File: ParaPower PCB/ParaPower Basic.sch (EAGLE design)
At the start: 4 parts, among them U1 ESP32_ESP-WROOM-32

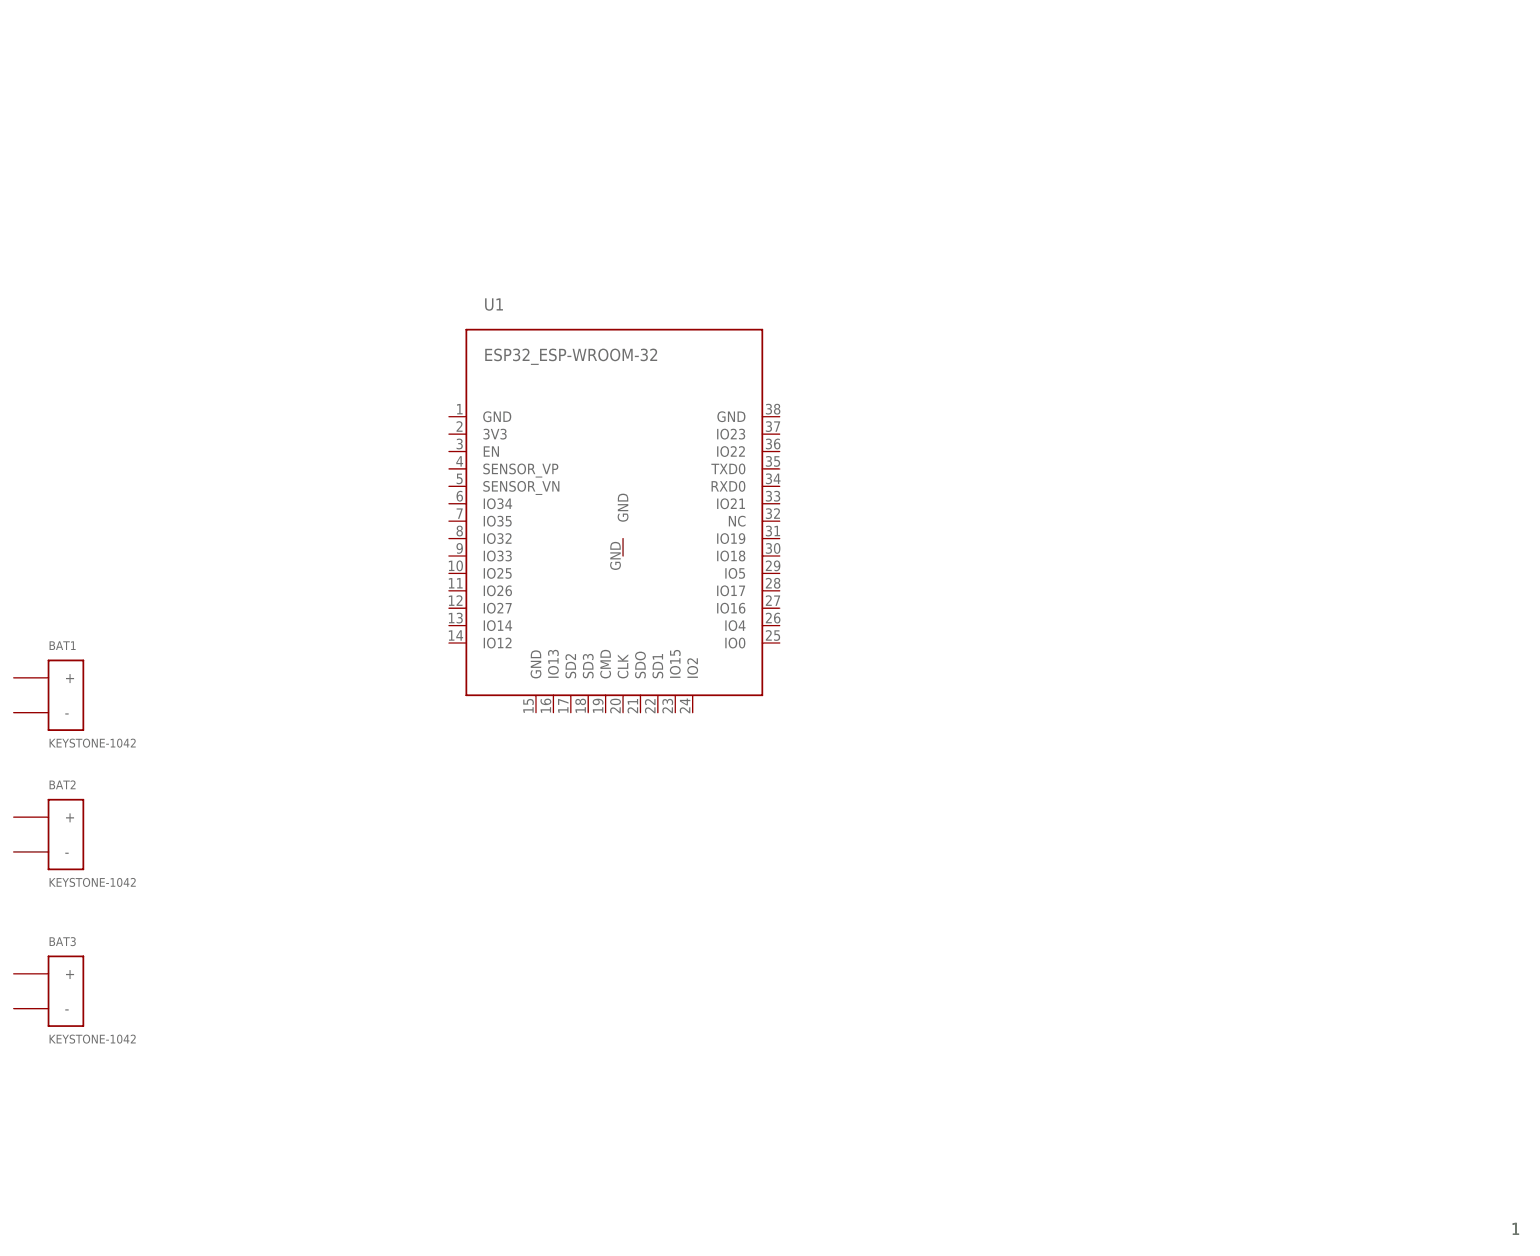
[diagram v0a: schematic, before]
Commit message: started to add voltage regulation section
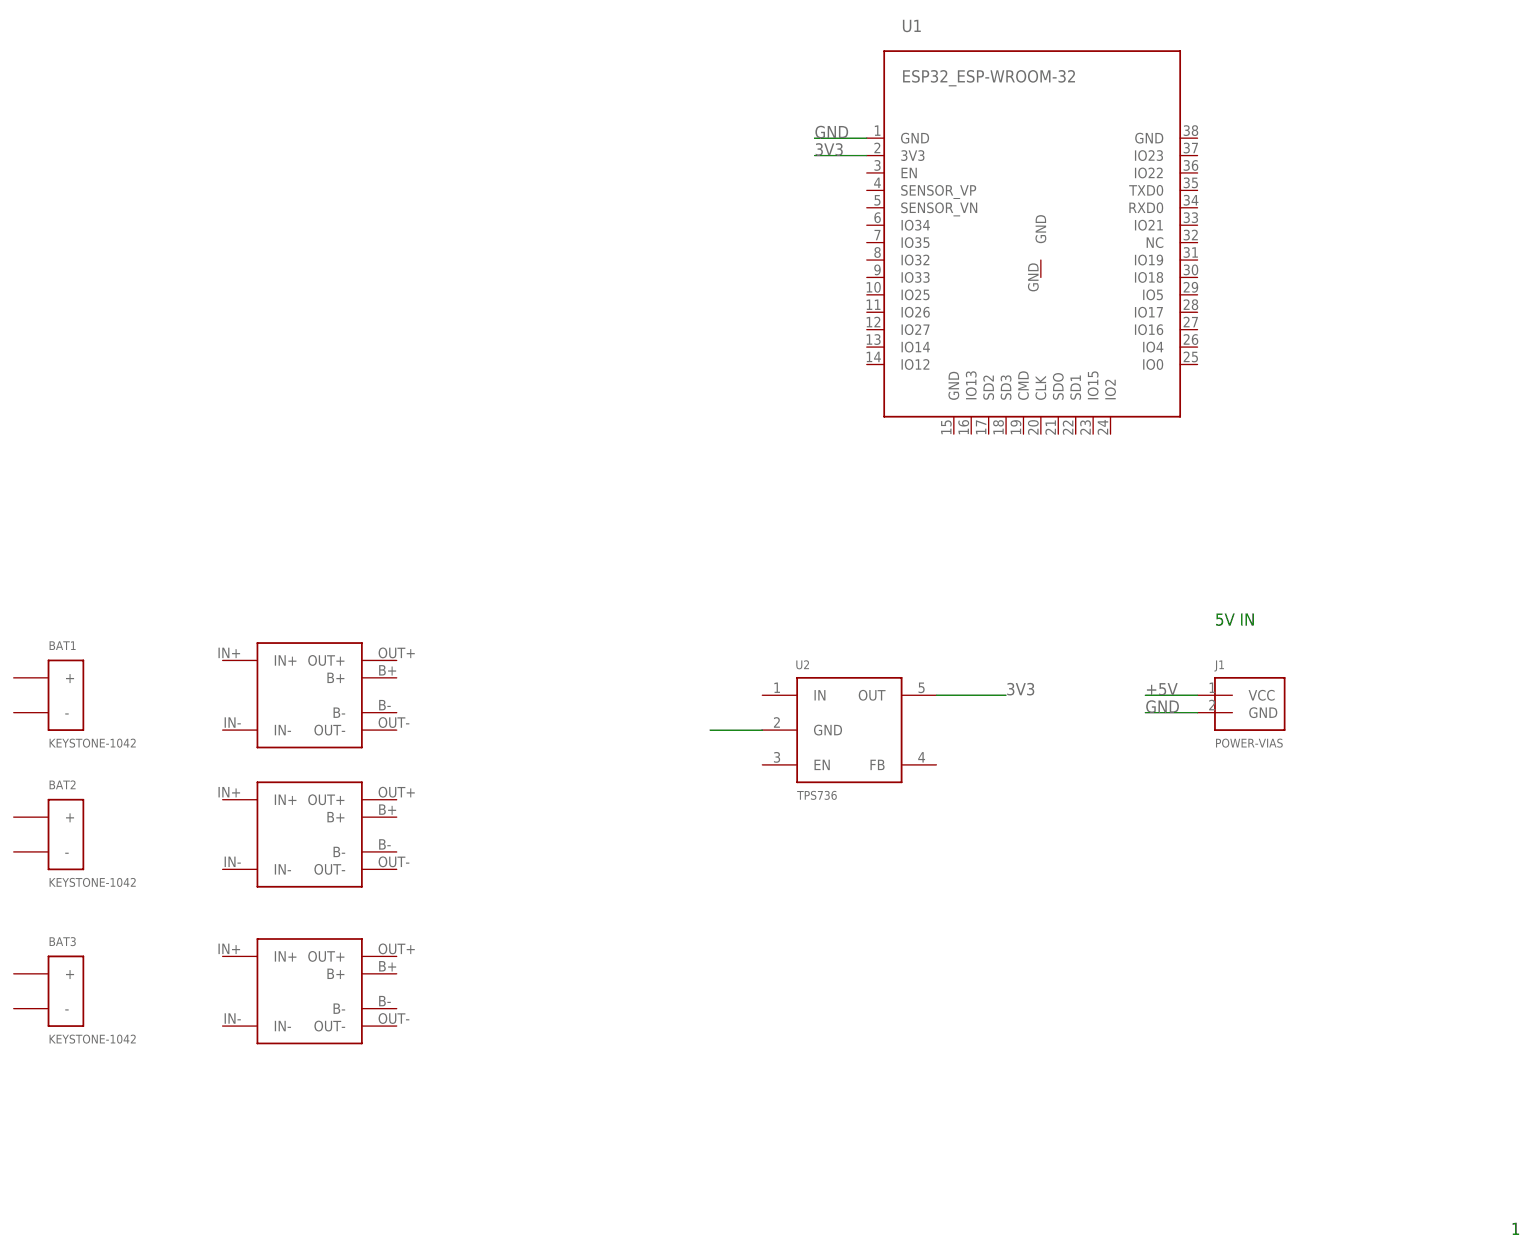
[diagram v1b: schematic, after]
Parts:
- added J1: POWER-VIAS, VanEagleLib:POWER-VIAS
- added U$1, U$2, U$3: TP4056-MODULE, userlib:TP4056-MODULE
- added U2: TPS736, VanEagleLib:TPS736
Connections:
- new net +5V: J1.VCC
- new net 3V3: U1.3V3, U2.OUT
- new net GND: J1.GND, U1.GND@1, U2.GND
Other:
- note added: "5V IN"
- moved on the sheet: U1
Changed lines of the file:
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@@
 <part name="U1" library="VCO - Pod Daughterboard v2.0" deviceset="ESP32_ESP-WROOM-32" device=""/>
 <part name="FRAME1" library="frames" deviceset="FRAME_A_L" device=""/>
+<part name="U$1" library="userlib" deviceset="TP4056-MODULE" device=""/>
+<part name="U$2" library="userlib" deviceset="TP4056-MODULE" device=""/>
+<part name="U$3" library="userlib" deviceset="TP4056-MODULE" device=""/>
+<part name="U2" library="VanEagleLib" library_urn="urn:adsk.eagle:library:5408729" deviceset="TPS736" device="" package3d_urn="urn:adsk.eagle:package:8894413/1"/>
+<part name="J1" library="VanEagleLib" library_urn="urn:adsk.eagle:library:5408729" deviceset="POWER-VIAS" device="" package3d_urn="urn:adsk.eagle:package:7547424/1"/>
 </parts>
 <sheets>
@@
 <plain>
 <text x="266.7" y="7.62" size="1.778" layer="91">1</text>
+<text x="223.52" y="96.52" size="1.778" layer="91">5V IN</text>
 </plain>
 <instances>
@@
 <attribute name="VALUE" x="53.34" y="35.56" size="1.27" layer="96"/>
 </instance>
-<instance part="U1" gate="G$1" x="129.54" y="124.46" smashed="yes">
-<attribute name="NAME" x="116.84" y="142.494" size="1.778" layer="95"/>
-<attribute name="VALUE" x="116.84" y="136.906" size="1.778" layer="96" align="top-left"/>
+<instance part="U1" gate="G$1" x="190.5" y="165.1" smashed="yes">
+<attribute name="NAME" x="177.8" y="183.134" size="1.778" layer="95"/>
+<attribute name="VALUE" x="177.8" y="177.546" size="1.778" layer="96" align="top-left"/>
 </instance>
 <instance part="FRAME1" gate="G$1" x="0" y="0" smashed="yes"/>
@@
 <attribute name="DRAWING_NAME" x="190.5" y="19.05" size="2.54" layer="94"/>
 </instance>
+<instance part="U$1" gate="G$1" x="91.44" y="86.36" smashed="yes"/>
+<instance part="U$2" gate="G$1" x="91.44" y="66.04" smashed="yes"/>
+<instance part="U$3" gate="G$1" x="91.44" y="43.18" smashed="yes"/>
+<instance part="U2" gate="G$1" x="170.18" y="81.28" smashed="yes">
+<attribute name="NAME" x="162.306" y="90.17" size="1.27" layer="95"/>
+<attribute name="VALUE" x="162.56" y="71.12" size="1.27" layer="96"/>
+</instance>
+<instance part="J1" gate="G$1" x="223.52" y="81.28" smashed="yes">
+<attribute name="NAME" x="223.52" y="90.17" size="1.27" layer="95"/>
+<attribute name="VALUE" x="223.52" y="78.74" size="1.27" layer="96"/>
+</instance>
 </instances>
 <busses>
 </busses>
 <nets>
+<net name="+5V" class="0">
+<segment>
+<pinref part="J1" gate="G$1" pin="VCC"/>
+<wire x1="220.98" y1="86.36" x2="213.36" y2="86.36" width="0.1524" layer="91"/>
+<label x="213.36" y="86.36" size="1.778" layer="95"/>
+</segment>
+</net>
+<net name="GND" class="0">
+<segment>
+<pinref part="J1" gate="G$1" pin="GND"/>
+<wire x1="220.98" y1="83.82" x2="213.36" y2="83.82" width="0.1524" layer="91"/>
+<label x="213.36" y="83.82" size="1.778" layer="95"/>
+</segment>
+<segment>
+<pinref part="U2" gate="G$1" pin="GND"/>
+<wire x1="157.48" y1="81.28" x2="149.86" y2="81.28" width="0.1524" layer="91"/>
+</segment>
+<segment>
+<pinref part="U1" gate="G$1" pin="GND@1"/>
+<wire x1="172.72" y1="167.64" x2="165.1" y2="167.64" width="0.1524" layer="91"/>
+<label x="165.1" y="167.64" size="1.778" layer="95"/>
+</segment>
+</net>
+<net name="3V3" class="0">
+<segment>
+<pinref part="U1" gate="G$1" pin="3V3"/>
+<wire x1="172.72" y1="165.1" x2="165.1" y2="165.1" width="0.1524" layer="91"/>
+<label x="165.1" y="165.1" size="1.778" layer="95"/>
+</segment>
+<segment>
+<pinref part="U2" gate="G$1" pin="OUT"/>
+<wire x1="182.88" y1="86.36" x2="193.04" y2="86.36" width="0.1524" layer="91"/>
+<label x="193.04" y="86.36" size="1.778" layer="95"/>
+</segment>
+</net>
 </nets>
 </sheet>
